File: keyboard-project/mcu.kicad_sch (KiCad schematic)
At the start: 0 parts

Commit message: ble update
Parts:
- added C10, C11, C12, C13, C20, C21, C22, C24, C26, C27, C28, C30, C9: 100n, symbol Device:C
- added C14, C19, C23, C25, C29: 4.7u, symbol Device:C
- added C15, C17: 1u, symbol Device:C
- added C16, C18: 10n, symbol Device:C
- added J2: TC2030, Connector:Tag-Connect_TC2030-IDC-NL_2x03_P1.27mm_Vertical, symbol Connector:TC2030
- added R15, R16, R17, R18, R19, R20, R21, R22, R23, R24, R25, R26: 10k, symbol Device:R_US
- added R27, R28: 4.7k, symbol Device:R_US
- added U5: STM32G474VETx, Package_QFP:LQFP-100_14x14mm_P0.5mm, symbol MCU_ST_STM32G4:STM32G474VETx
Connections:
- new net: C25.1, C26.2, U5.75 (VDD)
- new net: C13.2, C14.1, U5.24 (VDD)
- new net: C23.1, C24.2, U5.64 (VDD)
- new net: C19.1, C20.2, U5.49 (VDD)
- new net: C29.1, C30.2, U5.100 (VDD)
- new net +3.3V: C15.2, C16.1, C17.2, C18.1, C9.2, J2.1, R15.2, R16.2, R17.2, R18.2, R19.2, R20.2, R21.2, R22.2, R23.2, R24.2, R25.2, R27.2, R28.2, U5.36 (VREF+), U5.37 (VDDA), U5.6 (VBAT)
- new net BAT ADC: U5.18 (PC3)
- new net ENC 1 PHASE A: C11.1, R16.1, U5.20 (PA0)
- new net ENC 1 PHASE B: C12.1, R17.1, U5.21 (PA1)
- new net ENC 2 PHASE A: C27.1, R22.1, U5.65 (PC6)
- new net ENC 2 PHASE B: C28.1, R23.1, U5.66 (PC7)
- new net ENC 3 PHASE A: C21.1, R20.1, U5.59 (PD12)
- new net ENC 3 PHASE B: C22.1, R21.1, U5.60 (PD13)
- new net FT6336U INT: R15.1, U5.15 (PC0)
- new net FT6336U RSTN: U5.30 (PC4)
- new net GND: C10.1, C11.2, C12.2, C13.1, C14.2, C15.1, C16.2, C17.1, C18.2, C19.2, C20.1, C21.2, C22.2, C23.2, C24.1, C25.2, C26.1, C27.2, C28.2, C29.2, C30.1, C9.1, J2.5, R26.2, U5.23 (VSS), U5.35 (VSSA), U5.48 (VSS), U5.63 (VSS), U5.74 (VSS), U5.99 (VSS)
- new net I2C1_SCL: R26.1, R27.1, U5.95 (PB8)
- new net I2C1_SDA: R28.1, U5.96 (PB9)
- new net ILI9341 CSX: U5.45 (PE14)
- new net ILI9341 D/CX: U5.46 (PE15)
- new net ILI9341 RESX: U5.38 (PE7)
- new net ILI9341 backlight PWM: U5.69 (PA8)
- new net IS31FL3741A SDB: U5.25 (PA3)
- new net MCP73871 CE: U5.81 (PC12)
- new net MCP73871 PROG2: U5.32 (PB0)
- new net MCP73871 STAT1: R24.1, U5.67 (PC8)
- new net MCP73871 STAT2: R25.1, U5.68 (PC9)
- new net Matrix Col 0: U5.82 (PD0)
- new net Matrix Col 1: U5.83 (PD1)
- new net Matrix Col 10: U5.57 (PD10)
- new net Matrix Col 11: U5.58 (PD11)
- new net Matrix Col 12: U5.47 (PB10)
- new net Matrix Col 13: U5.50 (PB11)
- new net Matrix Col 14: U5.51 (PB12)
- new net Matrix Col 15: U5.79 (PC10)
- new net Matrix Col 16: U5.80 (PC11)
- new net Matrix Col 2: U5.84 (PD2)
- new net Matrix Col 3: U5.85 (PD3)
- new net Matrix Col 4: U5.86 (PD4)
- new net Matrix Col 5: U5.87 (PD5)
- new net Matrix Col 6: U5.88 (PD6)
- new net Matrix Col 7: U5.89 (PD7)
- new net Matrix Col 8: U5.55 (PD8)
- new net Matrix Col 9: U5.56 (PD9)
- new net Matrix Row 0: U5.39 (PE8)
- new net Matrix Row 1: U5.40 (PE9)
- new net Matrix Row 2: U5.41 (PE10)
- new net Matrix Row 3: U5.42 (PE11)
- new net Matrix Row 4: U5.43 (PE12)
- new net Matrix Row 5: U5.44 (PE13)
- new net NRST: C10.2, J2.6, U5.14 (PG10)
- new net PMW3360 NCS: R19.1, U5.26 (PA4)
- new net PWM3360 MOTION: R18.1, U5.22 (PA2)
- new net SPI1_MISO: U5.28 (PA6)
- new net SPI1_MOSI: U5.29 (PA7)
- new net SPI1_SCK: U5.27 (PA5)
- new net SPI2_MISO: U5.53 (PB14)
- new net SPI2_MOSI: U5.54 (PB15)
- new net SPI2_SCK: U5.52 (PB13)
- new net SWDCLK: J2.2, U5.77 (PA14)
- new net SWDIO: J2.4, U5.76 (PA13)
- new net USART1_RX: U5.71 (PA10)
- new net USART1_TX: U5.70 (PA9)
- new net USB D+: U5.73 (PA12)
- new net USB D-: U5.72 (PA11)
- new net VBUS Detect: U5.34 (PB2)
- new net nRF52840 RST: U5.16 (PC1)
- new net nRF52840 WAKE: U5.17 (PC2)
- no-connect marks 0 -> 23
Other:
- note added: "16MHz OSC. 12 I 13 O"
- note added: "48, 63, 74, 99 TO GND"
- note added: "5/3/26"
- note added: "MCU debug header"

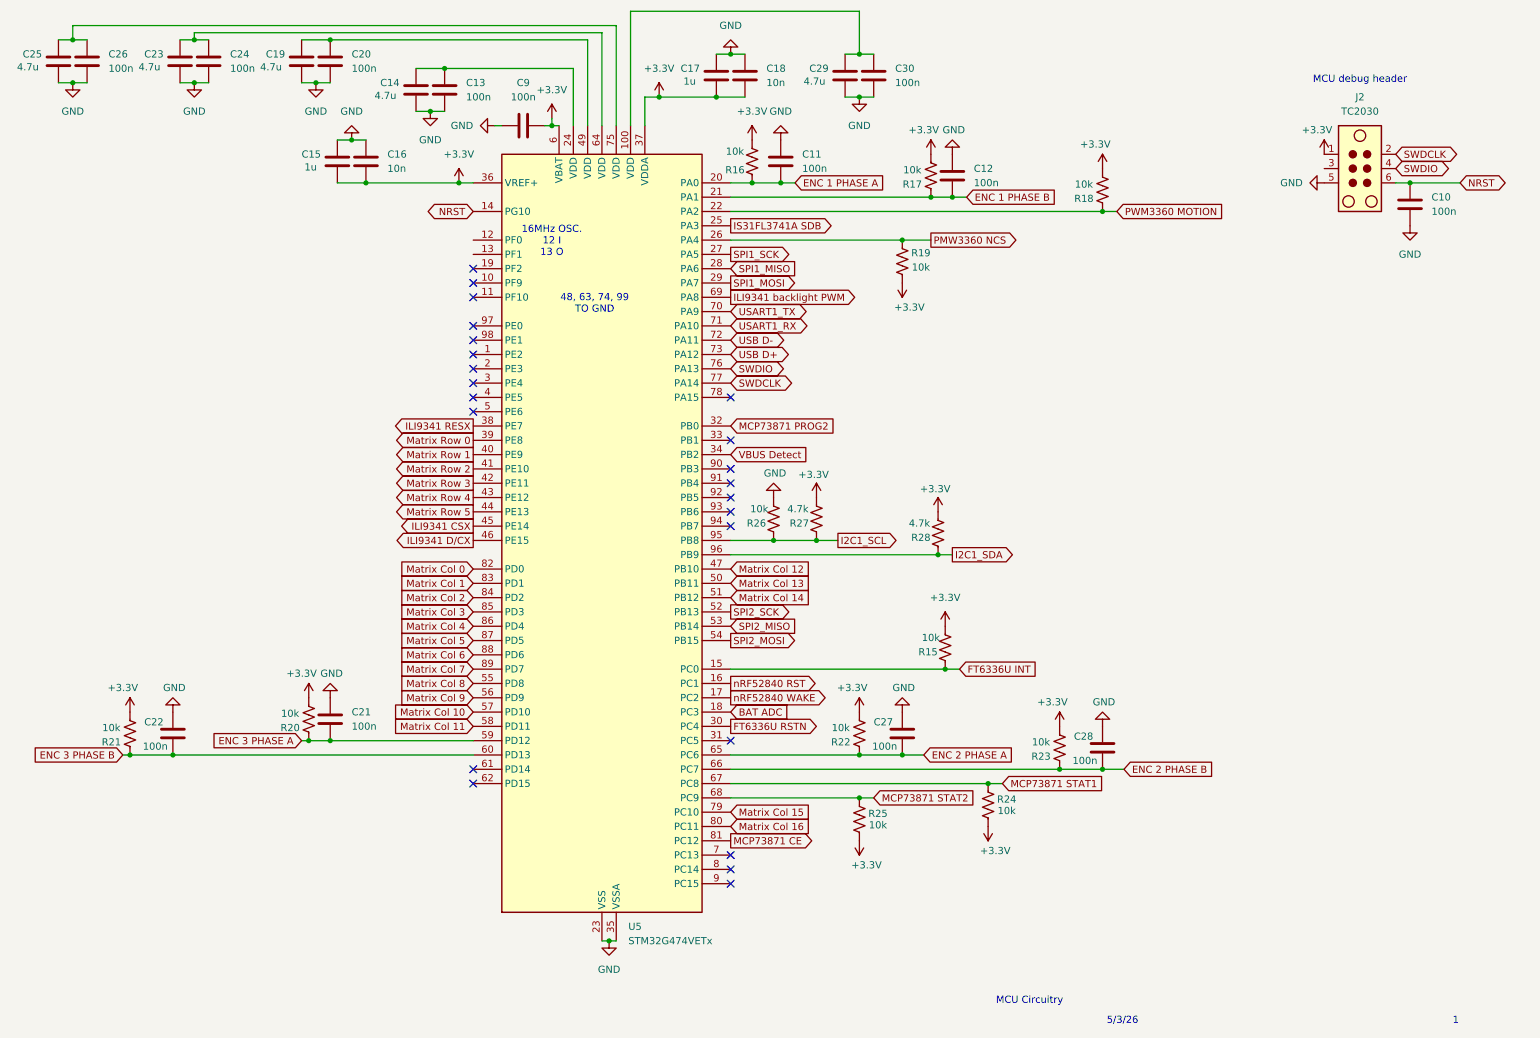
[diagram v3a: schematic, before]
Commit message: encoders, trackball, and display circuits
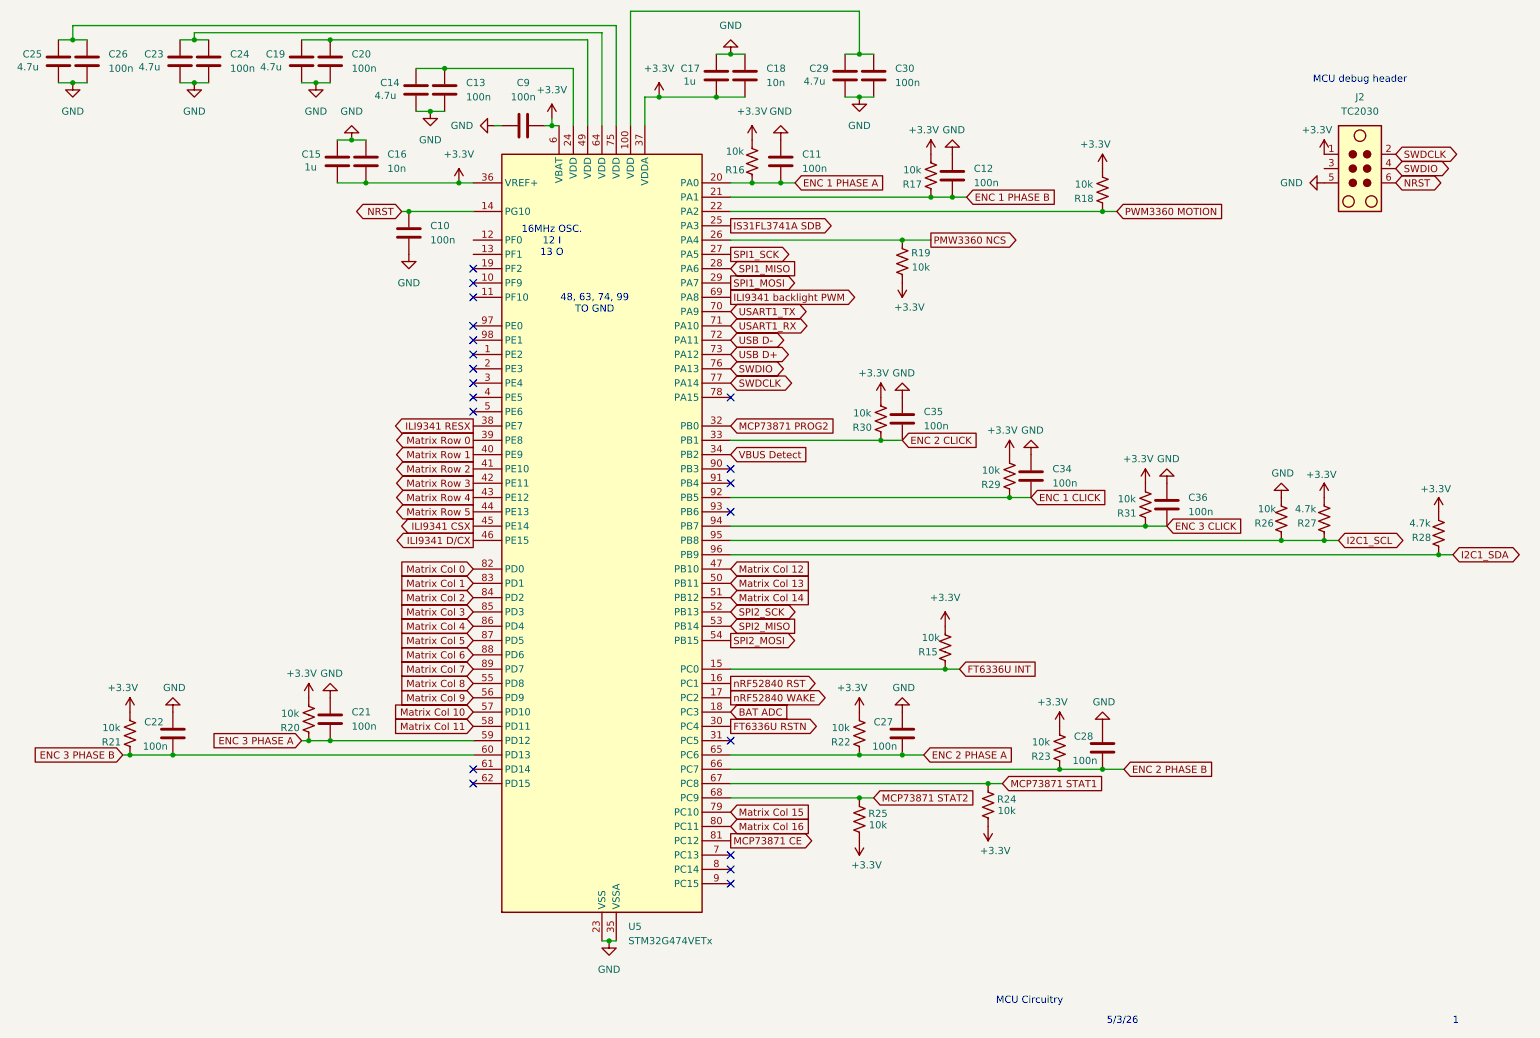
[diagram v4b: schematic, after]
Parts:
- added C34, C35, C36: 100n, symbol Device:C
- added R29, R30, R31: 10k, symbol Device:R_US
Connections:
- net +3.3V: now also R29.2, R30.2, R31.2
- net GND: now also C34.2, C35.2, C36.2
- net ENC 2 CLICK: now reaches U5.33 (PB1)
- net ENC 2 CLICK: now also C35.1, R30.1
- net ENC 1 CLICK: now reaches U5.92 (PB5)
- net ENC 1 CLICK: now also C34.1, R29.1
- net ENC 3 CLICK: now reaches U5.94 (PB7)
- net ENC 3 CLICK: now also C36.1, R31.1
- no-connect marks 23 -> 20
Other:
- moved on the sheet: R26, R27, R28

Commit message: res and cap footprints
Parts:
- C10, C11, C12, C13, C14, C15, C16, C17, C18, C19, C20, C21, C22, C23, C24, C25, C26, C27, C28, C29, C30, C34, C35, C36, C9: footprint (none) -> Capacitor_SMD:C_1206_3216Metric_Pad1.33x1.80mm_HandSolder
- R15, R16, R17, R18, R19, R20, R21, R22, R23, R24, R25, R26, R27, R28, R29, R30, R31: footprint (none) -> Resistor_SMD:R_1206_3216Metric_Pad1.30x1.75mm_HandSolder
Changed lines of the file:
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@@
 			)
 		)
-		(property "Footprint" ""
+		(property "Footprint" "Resistor_SMD:R_1206_3216Metric_Pad1.30x1.75mm_HandSolder"
 			(at 178.054 126.746 90)
 			(hide yes)
@@
 			)
 		)
-		(property "Footprint" ""
+		(property "Footprint" "Resistor_SMD:R_1206_3216Metric_Pad1.30x1.75mm_HandSolder"
 			(at 189.484 96.266 90)
 			(hide yes)
@@
 			)
 		)
-		(property "Footprint" ""
+		(property "Footprint" "Capacitor_SMD:C_1206_3216Metric_Pad1.33x1.80mm_HandSolder"
 			(at 25.7048 19.05 0)
 			(hide yes)
@@
 			)
 		)
-		(property "Footprint" ""
+		(property "Footprint" "Resistor_SMD:R_1206_3216Metric_Pad1.30x1.75mm_HandSolder"
 			(at 187.706 155.194 90)
 			(hide yes)
@@
 			)
 		)
-		(property "Footprint" ""
+		(property "Footprint" "Capacitor_SMD:C_1206_3216Metric_Pad1.33x1.80mm_HandSolder"
 			(at 82.8548 49.53 0)
 			(hide yes)
@@
 			)
 		)
-		(property "Footprint" ""
+		(property "Footprint" "Resistor_SMD:R_1206_3216Metric_Pad1.30x1.75mm_HandSolder"
 			(at 33.274 141.986 90)
 			(hide yes)
@@
 			)
 		)
-		(property "Footprint" ""
+		(property "Footprint" "Capacitor_SMD:C_1206_3216Metric_Pad1.33x1.80mm_HandSolder"
 			(at 86.0552 31.75 0)
 			(hide yes)
@@
 			)
 		)
-		(property "Footprint" ""
+		(property "Footprint" "Capacitor_SMD:C_1206_3216Metric_Pad1.33x1.80mm_HandSolder"
 			(at 217.4748 97.79 0)
 			(hide yes)
@@
 			)
 		)
-		(property "Footprint" ""
+		(property "Footprint" "Capacitor_SMD:C_1206_3216Metric_Pad1.33x1.80mm_HandSolder"
 			(at 193.3448 92.71 0)
 			(hide yes)
@@
 			)
 		)
-		(property "Footprint" ""
+		(property "Footprint" "Capacitor_SMD:C_1206_3216Metric_Pad1.33x1.80mm_HandSolder"
 			(at 44.1452 26.67 0)
 			(hide yes)
@@
 			)
 		)
-		(property "Footprint" ""
+		(property "Footprint" "Capacitor_SMD:C_1206_3216Metric_Pad1.33x1.80mm_HandSolder"
 			(at 72.0852 44.45 0)
 			(hide yes)
@@
 			)
 		)
-		(property "Footprint" ""
+		(property "Footprint" "Resistor_SMD:R_1206_3216Metric_Pad1.30x1.75mm_HandSolder"
 			(at 162.814 141.986 90)
 			(hide yes)
@@
 			)
 		)
-		(property "Footprint" ""
+		(property "Footprint" "Resistor_SMD:R_1206_3216Metric_Pad1.30x1.75mm_HandSolder"
 			(at 164.846 157.734 90)
 			(hide yes)
@@
 			)
 		)
-		(property "Footprint" ""
+		(property "Footprint" "Capacitor_SMD:C_1206_3216Metric_Pad1.33x1.80mm_HandSolder"
 			(at 68.8848 19.05 0)
 			(hide yes)
@@
 			)
 		)
-		(property "Footprint" ""
+		(property "Footprint" "Resistor_SMD:R_1206_3216Metric_Pad1.30x1.75mm_HandSolder"
 			(at 237.744 103.886 90)
 			(hide yes)
@@
 			)
 		)
-		(property "Footprint" ""
+		(property "Footprint" "Resistor_SMD:R_1206_3216Metric_Pad1.30x1.75mm_HandSolder"
 			(at 172.466 58.674 90)
 			(hide yes)
@@
 			)
 		)
-		(property "Footprint" ""
+		(property "Footprint" "Capacitor_SMD:C_1206_3216Metric_Pad1.33x1.80mm_HandSolder"
 			(at 22.5552 26.67 0)
 			(hide yes)
@@
 			)
 		)
-		(property "Footprint" ""
+		(property "Footprint" "Capacitor_SMD:C_1206_3216Metric_Pad1.33x1.80mm_HandSolder"
 			(at 206.0448 140.97 0)
 			(hide yes)
@@
 			)
 		)
-		(property "Footprint" ""
+		(property "Footprint" "Resistor_SMD:R_1206_3216Metric_Pad1.30x1.75mm_HandSolder"
 			(at 175.514 42.926 90)
 			(hide yes)
@@
 			)
 		)
-		(property "Footprint" ""
+		(property "Footprint" "Capacitor_SMD:C_1206_3216Metric_Pad1.33x1.80mm_HandSolder"
 			(at 68.8848 135.89 0)
 			(hide yes)
@@
 			)
 		)
-		(property "Footprint" ""
+		(property "Footprint" "Capacitor_SMD:C_1206_3216Metric_Pad1.33x1.80mm_HandSolder"
 			(at 47.2948 19.05 0)
 			(hide yes)
@@
 			)
 		)
-		(property "Footprint" ""
+		(property "Footprint" "Capacitor_SMD:C_1206_3216Metric_Pad1.33x1.80mm_HandSolder"
 			(at 139.3952 29.21 0)
 			(hide yes)
@@
 			)
 		)
-		(property "Footprint" ""
+		(property "Footprint" "Capacitor_SMD:C_1206_3216Metric_Pad1.33x1.80mm_HandSolder"
 			(at 75.2348 36.83 0)
 			(hide yes)
@@
 			)
 		)
-		(property "Footprint" ""
+		(property "Footprint" "Capacitor_SMD:C_1206_3216Metric_Pad1.33x1.80mm_HandSolder"
 			(at 179.3748 39.37 0)
 			(hide yes)
@@
 			)
 		)
-		(property "Footprint" ""
+		(property "Footprint" "Capacitor_SMD:C_1206_3216Metric_Pad1.33x1.80mm_HandSolder"
 			(at 142.5448 21.59 0)
 			(hide yes)
@@
 			)
 		)
-		(property "Footprint" ""
+		(property "Footprint" "Resistor_SMD:R_1206_3216Metric_Pad1.30x1.75mm_HandSolder"
 			(at 265.684 106.426 90)
 			(hide yes)
@@
 			)
 		)
-		(property "Footprint" ""
+		(property "Footprint" "Capacitor_SMD:C_1206_3216Metric_Pad1.33x1.80mm_HandSolder"
 			(at 148.8948 36.83 0)
 			(hide yes)
@@
 			)
 		)
-		(property "Footprint" ""
+		(property "Footprint" "Capacitor_SMD:C_1206_3216Metric_Pad1.33x1.80mm_HandSolder"
 			(at 89.2048 24.13 0)
 			(hide yes)
@@
 			)
 		)
-		(property "Footprint" ""
+		(property "Footprint" "Resistor_SMD:R_1206_3216Metric_Pad1.30x1.75mm_HandSolder"
 			(at 166.624 86.106 90)
 			(hide yes)
@@
 			)
 		)
-		(property "Footprint" ""
+		(property "Footprint" "Capacitor_SMD:C_1206_3216Metric_Pad1.33x1.80mm_HandSolder"
 			(at 107.95 33.3248 0)
 			(hide yes)
@@
 			)
 		)
-		(property "Footprint" ""
+		(property "Footprint" "Capacitor_SMD:C_1206_3216Metric_Pad1.33x1.80mm_HandSolder"
 			(at 170.4848 82.55 0)
 			(hide yes)
@@
 			)
 		)
-		(property "Footprint" ""
+		(property "Footprint" "Resistor_SMD:R_1206_3216Metric_Pad1.30x1.75mm_HandSolder"
 			(at 245.364 103.886 90)
 			(hide yes)
@@
 			)
 		)
-		(property "Footprint" ""
+		(property "Footprint" "Capacitor_SMD:C_1206_3216Metric_Pad1.33x1.80mm_HandSolder"
 			(at 65.7352 26.67 0)
 			(hide yes)
@@
 			)
 		)
-		(property "Footprint" ""
+		(property "Footprint" "Capacitor_SMD:C_1206_3216Metric_Pad1.33x1.80mm_HandSolder"
 			(at 40.9448 138.43 0)
 			(hide yes)
@@
 			)
 		)
-		(property "Footprint" ""
+		(property "Footprint" "Resistor_SMD:R_1206_3216Metric_Pad1.30x1.75mm_HandSolder"
 			(at 143.764 40.386 90)
 			(hide yes)
@@
 			)
 		)
-		(property "Footprint" ""
+		(property "Footprint" "Capacitor_SMD:C_1206_3216Metric_Pad1.33x1.80mm_HandSolder"
 			(at 170.4848 138.43 0)
 			(hide yes)
@@
 			)
 		)
-		(property "Footprint" ""
+		(property "Footprint" "Capacitor_SMD:C_1206_3216Metric_Pad1.33x1.80mm_HandSolder"
 			(at 162.2552 29.21 0)
 			(hide yes)
@@
 			)
 		)
-		(property "Footprint" ""
+		(property "Footprint" "Resistor_SMD:R_1206_3216Metric_Pad1.30x1.75mm_HandSolder"
 			(at 213.614 101.346 90)
 			(hide yes)
@@
 			)
 		)
-		(property "Footprint" ""
+		(property "Footprint" "Resistor_SMD:R_1206_3216Metric_Pad1.30x1.75mm_HandSolder"
 			(at 198.374 144.526 90)
 			(hide yes)
@@
 			)
 		)
-		(property "Footprint" ""
+		(property "Footprint" "Resistor_SMD:R_1206_3216Metric_Pad1.30x1.75mm_HandSolder"
 			(at 205.994 45.466 90)
 			(hide yes)
@@
 			)
 		)
-		(property "Footprint" ""
+		(property "Footprint" "Resistor_SMD:R_1206_3216Metric_Pad1.30x1.75mm_HandSolder"
 			(at 65.024 139.446 90)
 			(hide yes)
@@
 			)
 		)
-		(property "Footprint" ""
+		(property "Footprint" "Capacitor_SMD:C_1206_3216Metric_Pad1.33x1.80mm_HandSolder"
 			(at 165.4048 21.59 0)
 			(hide yes)
